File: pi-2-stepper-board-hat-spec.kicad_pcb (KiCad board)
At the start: 2 copper layers, 65 x 56 mm, 38 parts, among them CON1 DC12v, P1 Servo, P10 BK_FEED_BYPASS, P2 Endstop1, P3 Endstop2, P4 Stepper1, P5 Stepper2, P6 COM, P7 Aux1 (SPI), P8 Aux2 (I2C)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

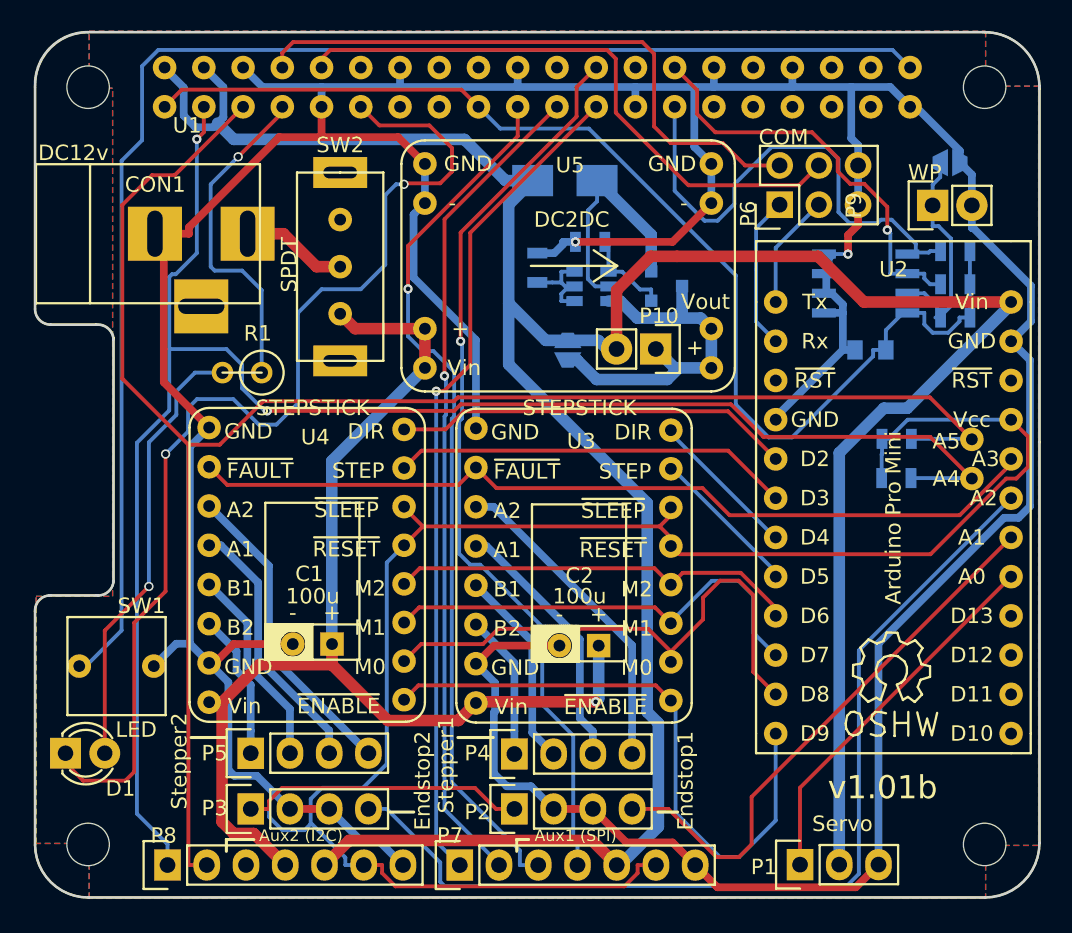
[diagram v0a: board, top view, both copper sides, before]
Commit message: Expanded aux ports
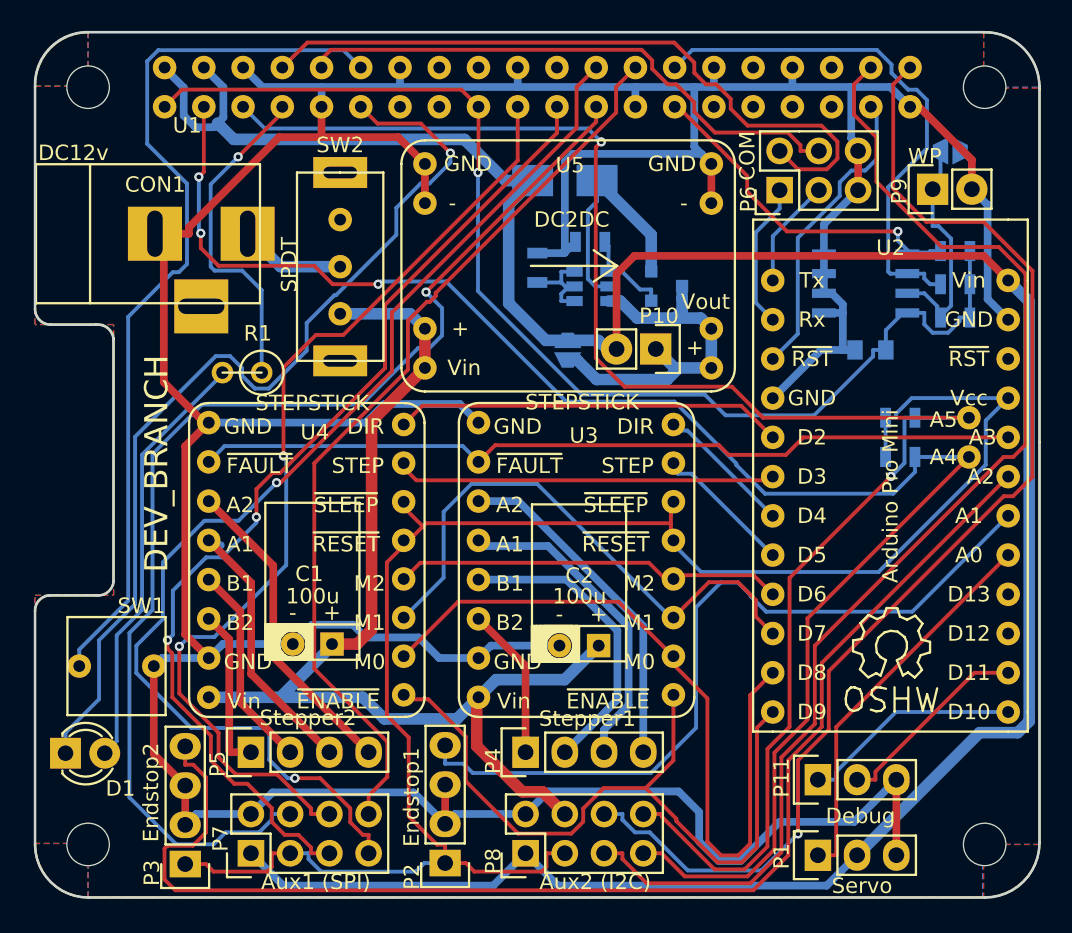
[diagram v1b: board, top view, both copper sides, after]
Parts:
- added P11: Debug, Pin_Headers:Pin_Header_Straight_1x03, F.Cu at (127.4, 92.4)
- D1: value LED -> Bi_colour_LED
- P7, P8: footprint Pin_Headers:Pin_Header_Straight_1x07 -> Pin_Headers:Pin_Header_Straight_2x04
- moved P8 23.2 mm to (108.5, 97.2)
- moved P7 13.5 mm to (90.7, 97.2)
- moved OSH2 5.99 mm to (134.1, 78.7)
- moved P2 5.69 mm to (103.3, 97.8), turned to 180 degrees
- moved P3 5.54 mm to (86.5, 97.9), turned to 180 degrees
- moved OSH1 1.59 mm to (132.2, 83.8)
- moved U2 1.41 mm to (132.1, 74.0)
- moved R2 1.39 mm to (132.8, 71.5)
- moved R3 1.39 mm to (132.8, 69.0)
- moved P1 1.31 mm to (127.4, 97.3)
- moved P9 1.05 mm to (134.9, 54.2)
- moved P6 0.94 mm to (125.0, 54.2)
- moved JP1 0.76 mm to (136.0, 51.7)
- moved P4 0.73 mm to (108.5, 90.6)
- moved U3 0.40 mm to (112.3, 76.9)
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- renumbered REF** to OSH1, REF** to OSH2
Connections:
- P7 pad 1: /SPI0_SCLK -> /Pi5v
- P7 pad 2: /SPI0_MISO -> GND
- P7 pad 3: /SPI0_MOSI -> /3v3
- P7 pad 4: /SPI0_CE0 -> /SPI0_SCLK
- P7 pad 5: /Pi5v -> /SPI0_MISO
- P7 pad 6: /3v3 -> /SPI0_MOSI
- P7 pad 7: GND -> /SPI0_CE0
- P8 pad 1: /SDA -> /Pi5v
- P8 pad 2: /SCL -> GND
- P8 pad 3: Net-(P8-Pad3) -> /3v3
- P8 pad 5: /Pi5v -> /GPIO20
- P8 pad 6: /3v3 -> /GPIO21
- P8 pad 7: GND -> /SDA
- SW1 pad 1: /GPIO21 -> /GPIO18
- U1 pad 12: Net-(U1-Pad12) -> /GPIO18
- U1 pad 37: Net-(U1-Pad37) -> /ArdRST
- U1 pad 38: Net-(U1-Pad38) -> /GPIO20
- U2 pad 13: Net-(U2-Pad13) -> /D10
- U2 pad 14: Net-(U2-Pad14) -> /D11
- U2 pad 3: Net-(U2-Pad3) -> /ArdRST
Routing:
- net /GPIO20: track 0.00 -> 78.3 mm
- net /SPI0_CE1: track 0.00 -> 59.5 mm
- net /GPIO18: track 0.00 -> 58.5 mm
- net /SPI0_SCLK: track 54.3 -> 77.3 mm
- net /ESTOP2: track 63.3 -> 83.6 mm
- net /ArdRST: track 0.00 -> 19.8 mm
- net /3v3: track 134.6 -> 115.4 mm
- net /Pi5v: track 187.5 -> 169.2 mm
- net /SPI0_CE0: track 58.9 -> 75.1 mm, vias 1 -> 2
- net /ESTOP1: track 36.2 -> 51.0 mm
- net /D10: track 0.00 -> 14.4 mm
- net /GPIO21: track 91.9 -> 77.9 mm, vias 0 -> 1
- net /M0: track 34.9 -> 48.8 mm
- net /D11: track 0.00 -> 13.0 mm
- net /SPI0_MISO: track 54.3 -> 65.8 mm, vias 1 -> 2
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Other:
- board text added: "DEV_BRANCH"
- board text added: "github.com/markjb/ pi-2-stepper-board"
- board text removed: "github.com/markjb/pi-2-stepper-board"
- board text removed: "v1.01b"
